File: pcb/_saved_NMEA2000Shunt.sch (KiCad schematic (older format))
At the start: 26 parts, among them IC101 ATTINY3224-SS, K101 Battery, P101 Temp1, P102 Prog, P103 CAN, P105 OLED, U101 MCP2515, U102 TJA1050, U103 NCP1117ST50T3G, U104 INA219-module, X101 8MHz

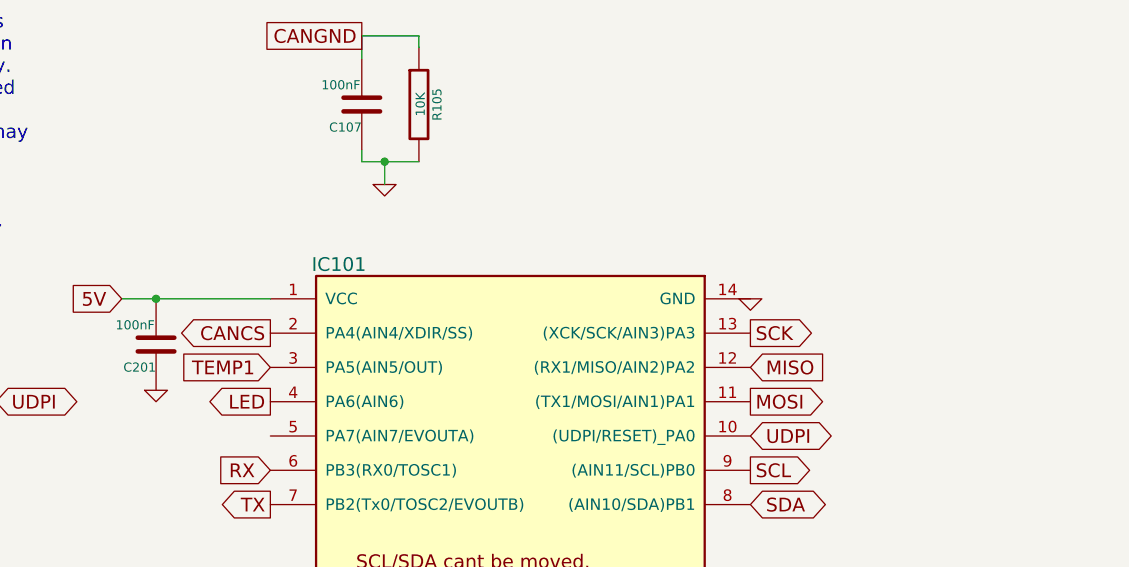
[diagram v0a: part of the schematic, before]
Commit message: Working version tested with Cansocket and canboat
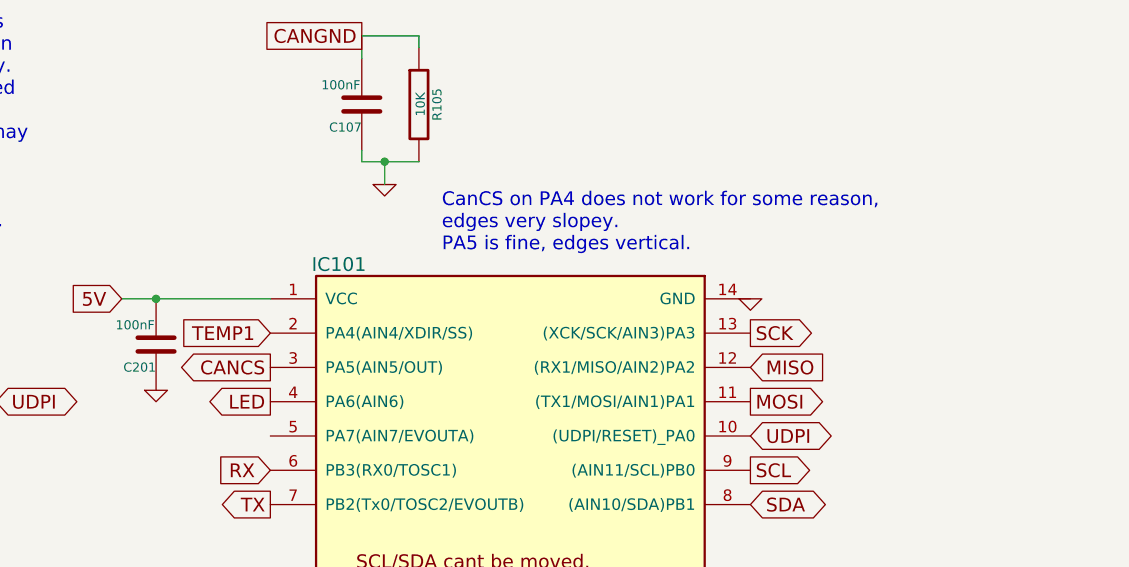
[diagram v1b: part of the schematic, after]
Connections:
- net CANCS: now also IC101.3 (PA5(AIN5/OUT)); no longer IC101.2 (PA4(AIN4/XDIR/SS))
- net TEMP1: now also IC101.2 (PA4(AIN4/XDIR/SS)); no longer IC101.3 (PA5(AIN5/OUT))
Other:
- note added: "CanCS on PA4 does not work for some reason,\nedges very slopey.\nPA5 is fine, edges vertical."
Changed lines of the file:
@@
 Text GLabel 5600 4050 2    60   Input ~ 0
 MISO
-Text GLabel 3500 3900 0    60   Output ~ 0
+Text GLabel 3500 4050 0    60   Output ~ 0
 CANCS
 Text GLabel 5600 4500 2    60   Output ~ 0
@@
 Text GLabel 5700 6450 2    60   BiDi ~ 0
 IN-
-Text GLabel 3500 4050 0    60   Input ~ 0
+Text GLabel 3500 3900 0    60   Input ~ 0
 TEMP1
 Text GLabel 3500 4200 0    60   Output ~ 0
@@
 Text GLabel 1550 6800 2    60   UnSpc ~ 0
 CANGND
+Text Notes 4250 3550 0    60   ~ 0
+CanCS on PA4 does not work for some reason,\nedges very slopey.\nPA5 is fine, edges vertical.
 $EndSCHEMATC
